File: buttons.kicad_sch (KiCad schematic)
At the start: 91 parts, among them SW1 TC002-N11AS2XT-RGB, SW10 TC002-N11AS2XT-RGB, SW11 TC002-N11AS2XT-RGB, SW12 TC002-N11AS2XT-RGB, SW13 TC002-N11AS2XT-RGB, SW2 TC002-N11AS2XT-RGB, SW3 TC002-N11AS2XT-RGB, SW4 TC002-N11AS2XT-RGB, SW5 TC002-N11AS2XT-RGB, SW6 TC002-N11AS2XT-RGB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

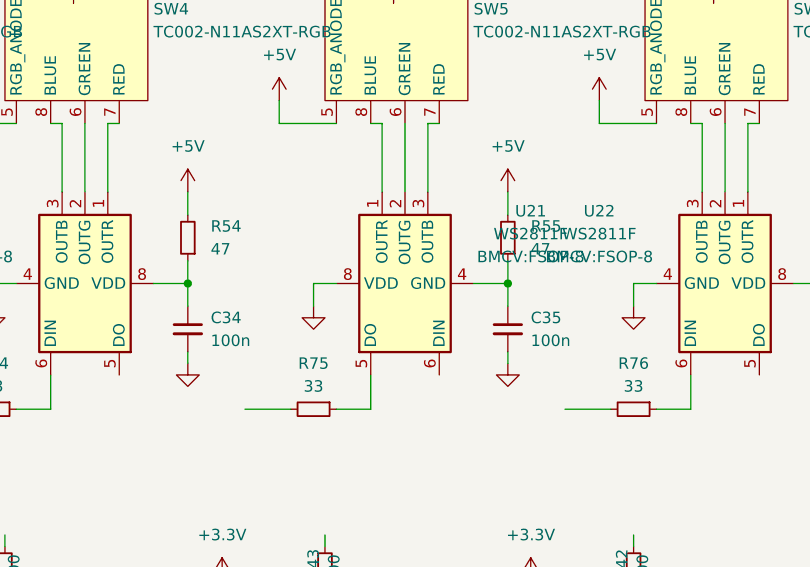
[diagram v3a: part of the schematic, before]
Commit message: routing progress (bottom buttons & encoders)
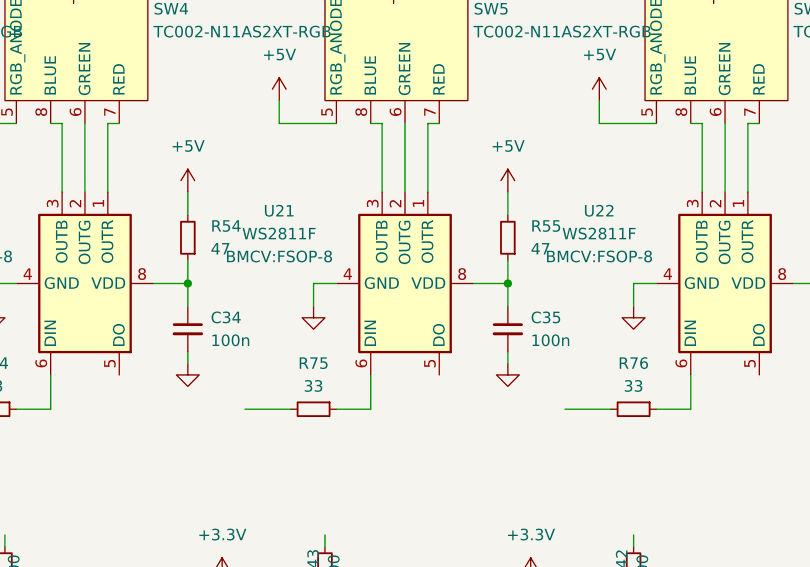
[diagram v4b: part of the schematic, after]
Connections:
- net GND: now also U21.4 (GND); no longer U21.8 (VDD)
- net at R75.1: now also U21.6 (DIN); no longer U21.5 (DO)
- net at SW5.7 (RED): now also U21.1 (OUTR); no longer U21.3 (OUTB)
- net at SW5.8 (BLUE): now also U21.3 (OUTB); no longer U21.1 (OUTR)
- net at C35.1, R55.1: now also U21.8 (VDD); no longer U21.4 (GND)
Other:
- moved on the sheet: U21
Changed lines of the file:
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@@
 	(symbol
 		(lib_id "BMCV:WS2811")
-		(at 196.85 68.58 90)
+		(at 196.85 68.58 270)
+		(mirror x)
 		(unit 1)
 		(exclude_from_sim no)
@@
 		(on_board yes)
 		(dnp no)
-		(fields_autoplaced yes)
 		(property "Reference" "U21"
-			(at 210.82 60.5438 90)
+			(at 182.88 60.5438 90)
 			(effects
 				(font
@@
 		)
 		(property "Value" "WS2811F"
-			(at 210.82 63.0838 90)
+			(at 182.88 63.0838 90)
 			(effects
 				(font
@@
 		)
 		(property "Footprint" "BMCV:FSOP-8"
-			(at 210.82 65.6238 90)
+			(at 182.88 65.6238 90)
 			(effects
 				(font
@@
 		)
 		(property "Datasheet" "https://cdn-shop.adafruit.com/datasheets/WS2811.pdf"
-			(at 190.5 73.66 0)
+			(at 203.2 73.66 0)
 			(effects
 				(font

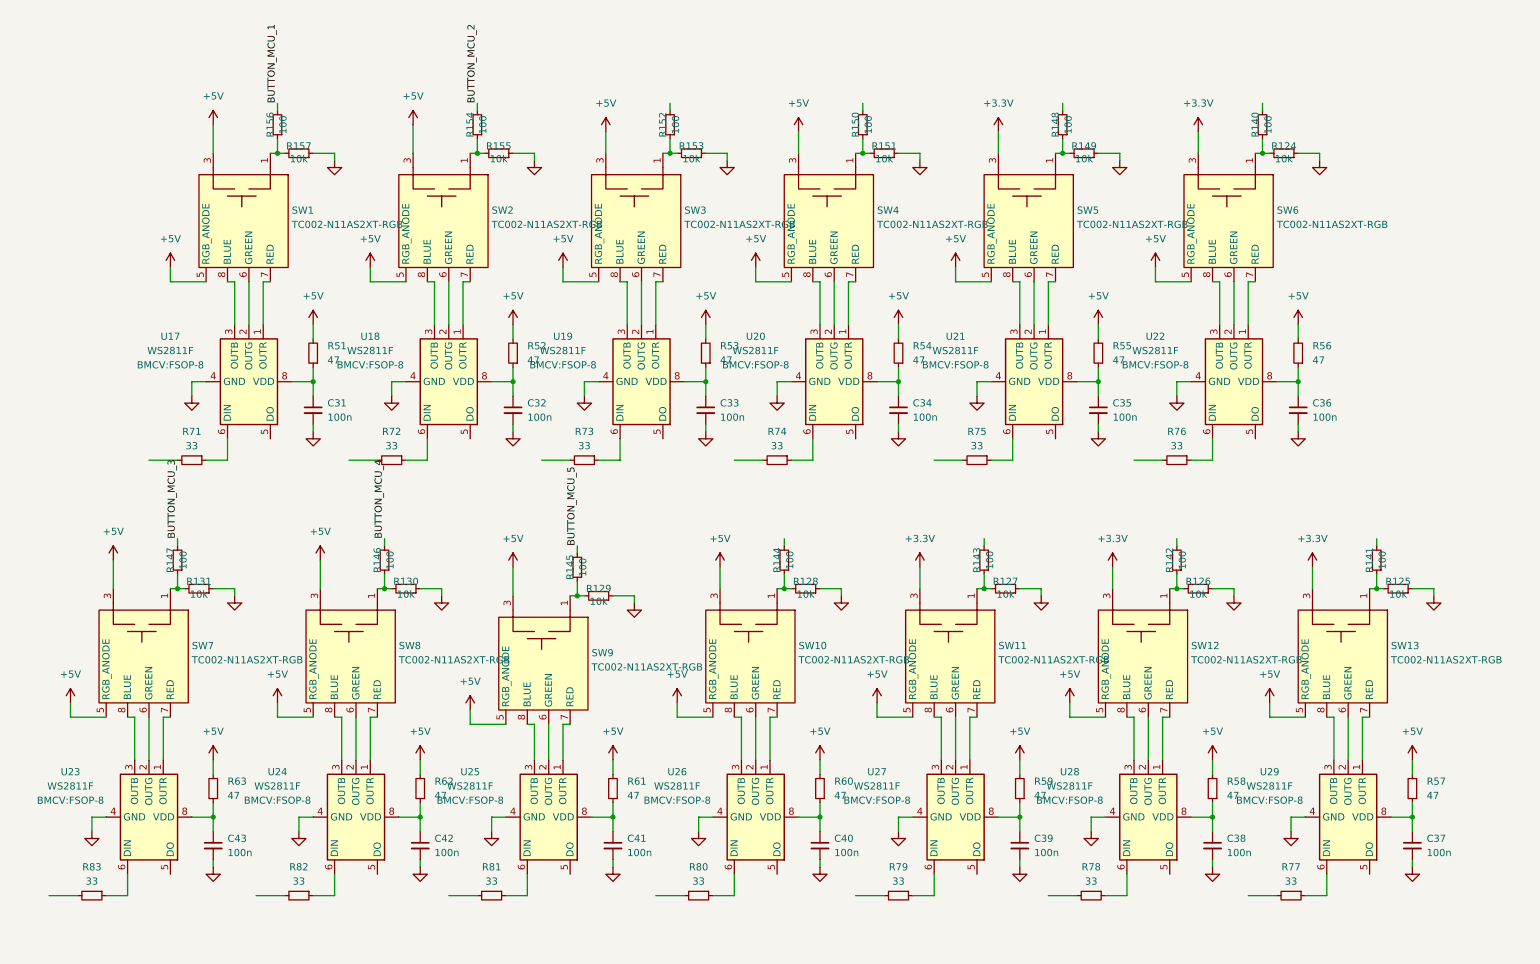
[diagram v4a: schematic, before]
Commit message: switches & led data routing
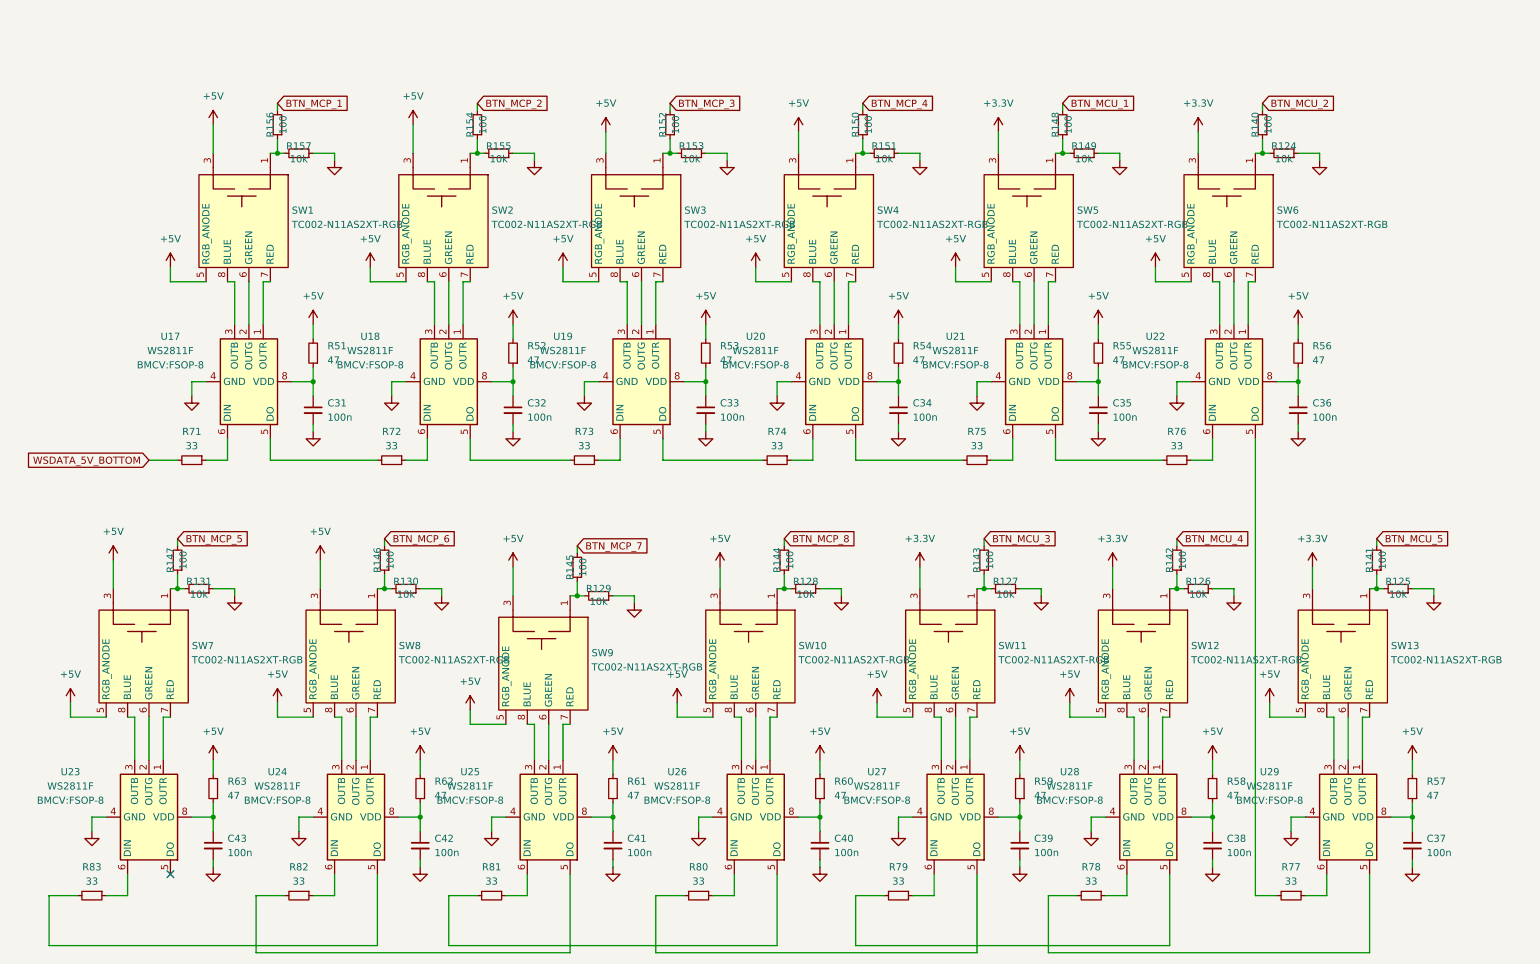
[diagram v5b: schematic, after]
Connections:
- net at U25.5 (DO): now also R82.2
- net BTN_MCP_4: now reaches R150.2
- net BTN_MCP_8: now reaches R144.2
- net at U26.5 (DO): now also R81.2
- net at R75.2: now also U20.5 (DO)
- net at R77.2: now also U22.5 (DO)
- net at R78.2: now also U29.5 (DO)
- net BTN_MCU_5: now reaches R141.2
- net at U28.5 (DO): now also R79.2
- net at R72.2: now also U17.5 (DO)
- net at R80.2: now also U27.5 (DO)
- net BTN_MCU_2: now reaches R140.2
- net BTN_MCU_3: now reaches R143.2
- net BTN_MCU_1: now reaches R148.2
- net at U18.5 (DO): now also R73.2
- net at U21.5 (DO): now also R76.2
- net at U19.5 (DO): now also R74.2
- net BTN_MCU_4: now reaches R142.2
- net WSDATA_5V_BOTTOM: now reaches R71.2
- net at R83.2: now also U24.5 (DO)
- net BTN_MCP_3: now reaches R152.2
- net BUTTON_MCU_1 renamed BTN_MCP_1
- net BUTTON_MCU_2 renamed BTN_MCP_2
- net BUTTON_MCU_3 renamed BTN_MCP_5
- net BUTTON_MCU_4 renamed BTN_MCP_6
- net BUTTON_MCU_5 renamed BTN_MCP_7
- no-connect marks 0 -> 1

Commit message: alpha
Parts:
- C31, C32, C33, C34, C35, C36, C37, C38, C39, C40, C41, C42, C43: LCSC Part # (none) -> C307331
- R124, R125, R126, R127, R128, R129, R130, R131, R149, R151, R153, R155, R157: LCSC Part # (none) -> C25744
- R140, R141, R142, R143, R144, R145, R146, R147, R148, R150, R152, R154, R156: LCSC Part # (none) -> C25076
- R51, R52, R53, R54, R55, R56, R57, R58, R59, R60, R61, R62, R63: value 47 -> 100; LCSC Part # (none) -> C25076
- R71, R72, R73, R74, R75, R76, R77, R78, R79, R80, R81, R82, R83: LCSC Part # (none) -> C25105
- SW1, SW10, SW11, SW12, SW13, SW2, SW3, SW4, SW5, SW6, SW7, SW8, SW9: now not fitted
- U17, U18, U19, U20, U21, U22, U23, U24, U25, U26, U27, U28, U29: LCSC Part # (none) -> C5446692

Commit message: update
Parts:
- SW1, SW10, SW11, SW12, SW13, SW2, SW3, SW4, SW5, SW6, SW7, SW8, SW9: now fitted
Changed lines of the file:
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@@
 		(in_bom yes)
 		(on_board yes)
-		(dnp yes)
+		(dnp no)
 		(fields_autoplaced yes)
 		(property "Reference" "SW12"
@@
 		(in_bom yes)
 		(on_board yes)
-		(dnp yes)
+		(dnp no)
 		(fields_autoplaced yes)
 		(property "Reference" "SW13"
@@
 		(in_bom yes)
 		(on_board yes)
-		(dnp yes)
+		(dnp no)
 		(fields_autoplaced yes)
 		(property "Reference" "SW4"
@@
 		(in_bom yes)
 		(on_board yes)
-		(dnp yes)
+		(dnp no)
 		(fields_autoplaced yes)
 		(property "Reference" "SW1"
@@
 		(in_bom yes)
 		(on_board yes)
-		(dnp yes)
+		(dnp no)
 		(fields_autoplaced yes)
 		(property "Reference" "SW5"
@@
 		(in_bom yes)
 		(on_board yes)
-		(dnp yes)
+		(dnp no)
 		(property "Reference" "SW10"
 			(at 154.94 115.5699 90)
@@
 		(in_bom yes)
 		(on_board yes)
-		(dnp yes)
+		(dnp no)
 		(fields_autoplaced yes)
 		(property "Reference" "SW7"
@@
 		(in_bom yes)
 		(on_board yes)
-		(dnp yes)
+		(dnp no)
 		(fields_autoplaced yes)
 		(property "Reference" "SW8"
@@
 		(in_bom yes)
 		(on_board yes)
-		(dnp yes)
+		(dnp no)
 		(fields_autoplaced yes)
 		(property "Reference" "SW3"
@@
 		(in_bom yes)
 		(on_board yes)
-		(dnp yes)
+		(dnp no)
 		(property "Reference" "SW11"
 			(at 190.5 115.5699 90)
@@
 		(in_bom yes)
 		(on_board yes)
-		(dnp yes)
+		(dnp no)
 		(fields_autoplaced yes)
 		(property "Reference" "SW6"
@@
 		(in_bom yes)
 		(on_board yes)
-		(dnp yes)
+		(dnp no)
 		(fields_autoplaced yes)
 		(property "Reference" "SW9"
@@
 		(in_bom yes)
 		(on_board yes)
-		(dnp yes)
+		(dnp no)
 		(fields_autoplaced yes)
 		(property "Reference" "SW2"

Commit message: first ordered verrsion
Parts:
- R51, R52, R53, R54, R55, R56, R57, R58, R59, R60, R61, R62, R63: value 100 -> 10; LCSC Part # C25076 -> C25077
